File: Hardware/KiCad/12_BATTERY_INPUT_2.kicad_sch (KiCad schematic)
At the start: 0 parts

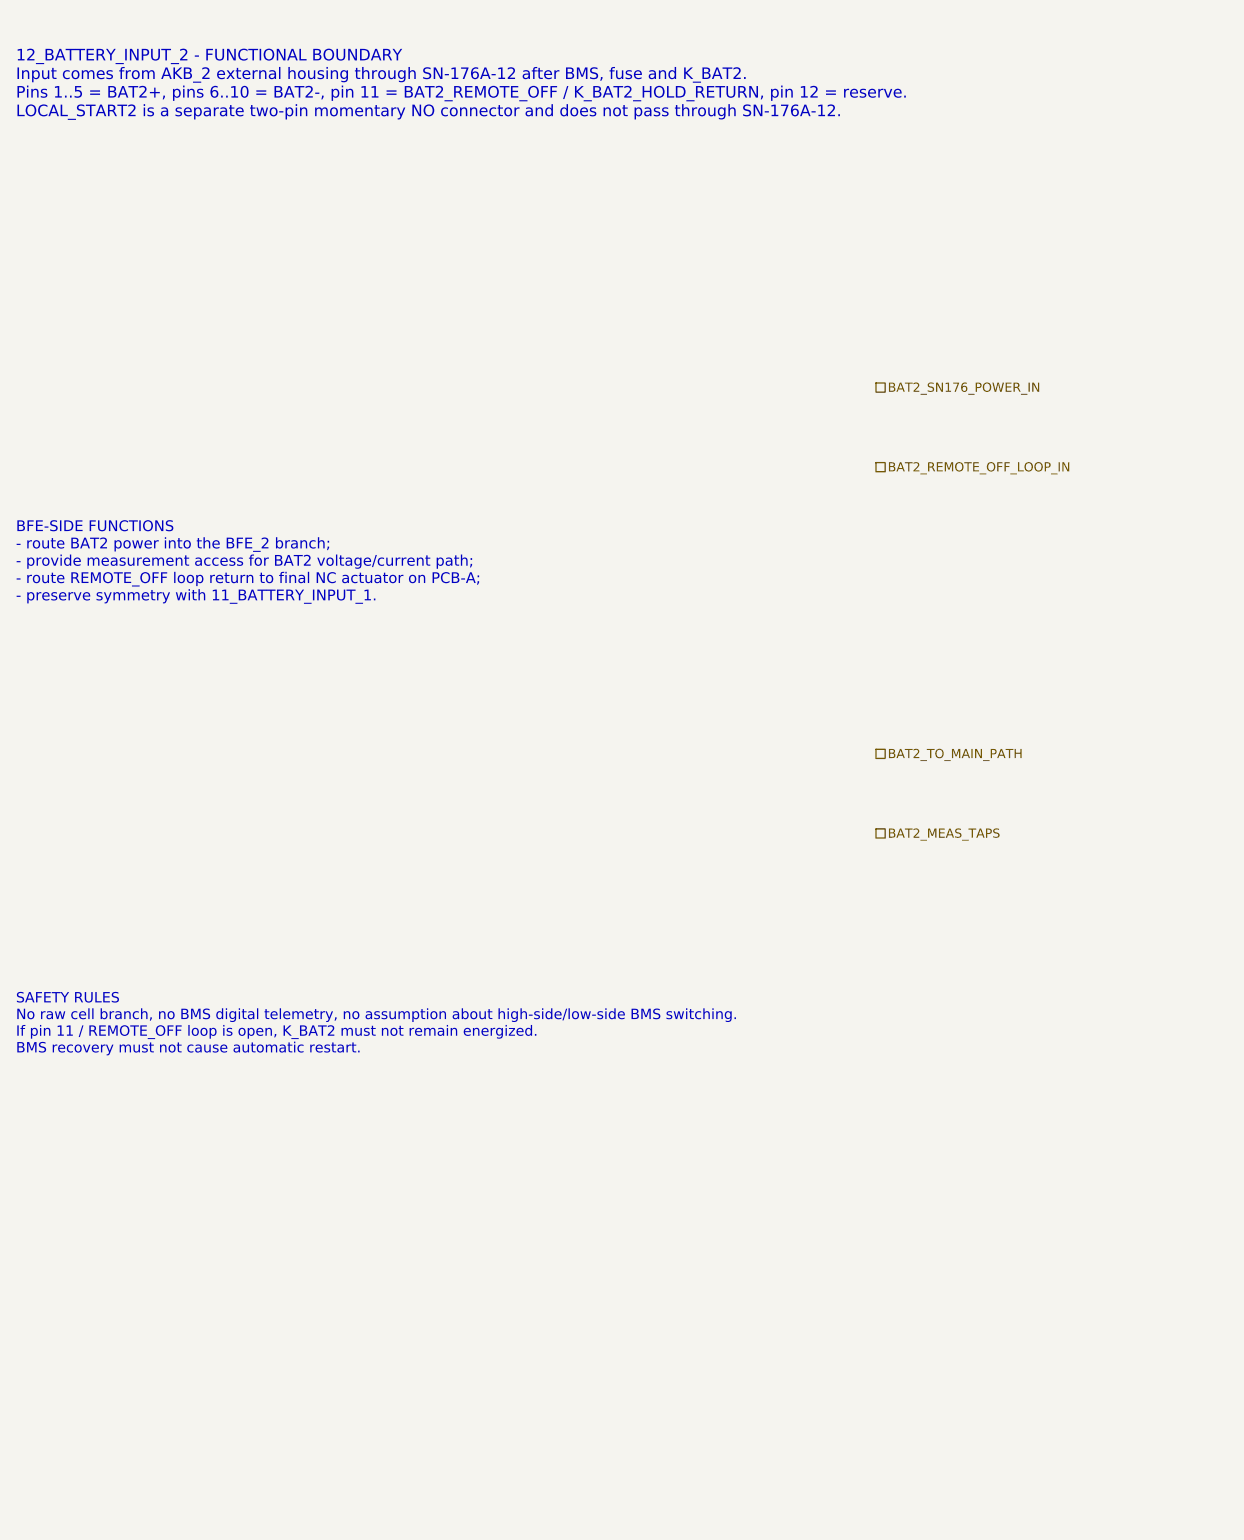
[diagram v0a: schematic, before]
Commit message: hardware: refine BFE inputs and hold-loop logic level B
Refine the first critical BFE sheets to Architecture Level B without selecting concrete components.

Included:
- BAT1/BAT2 SN-176A-12 positive/negative interface groups
- BAT1/BAT2 hold-loop return names
- hold-loop safe-state chain through EXT_KILL_NC and REMOTE_OFF_NC
- manifest update

No part numbers, footprints, PCB layout, relay technology, fuse values, current sensors or K_BATx/MAIN_SWx models are selected.
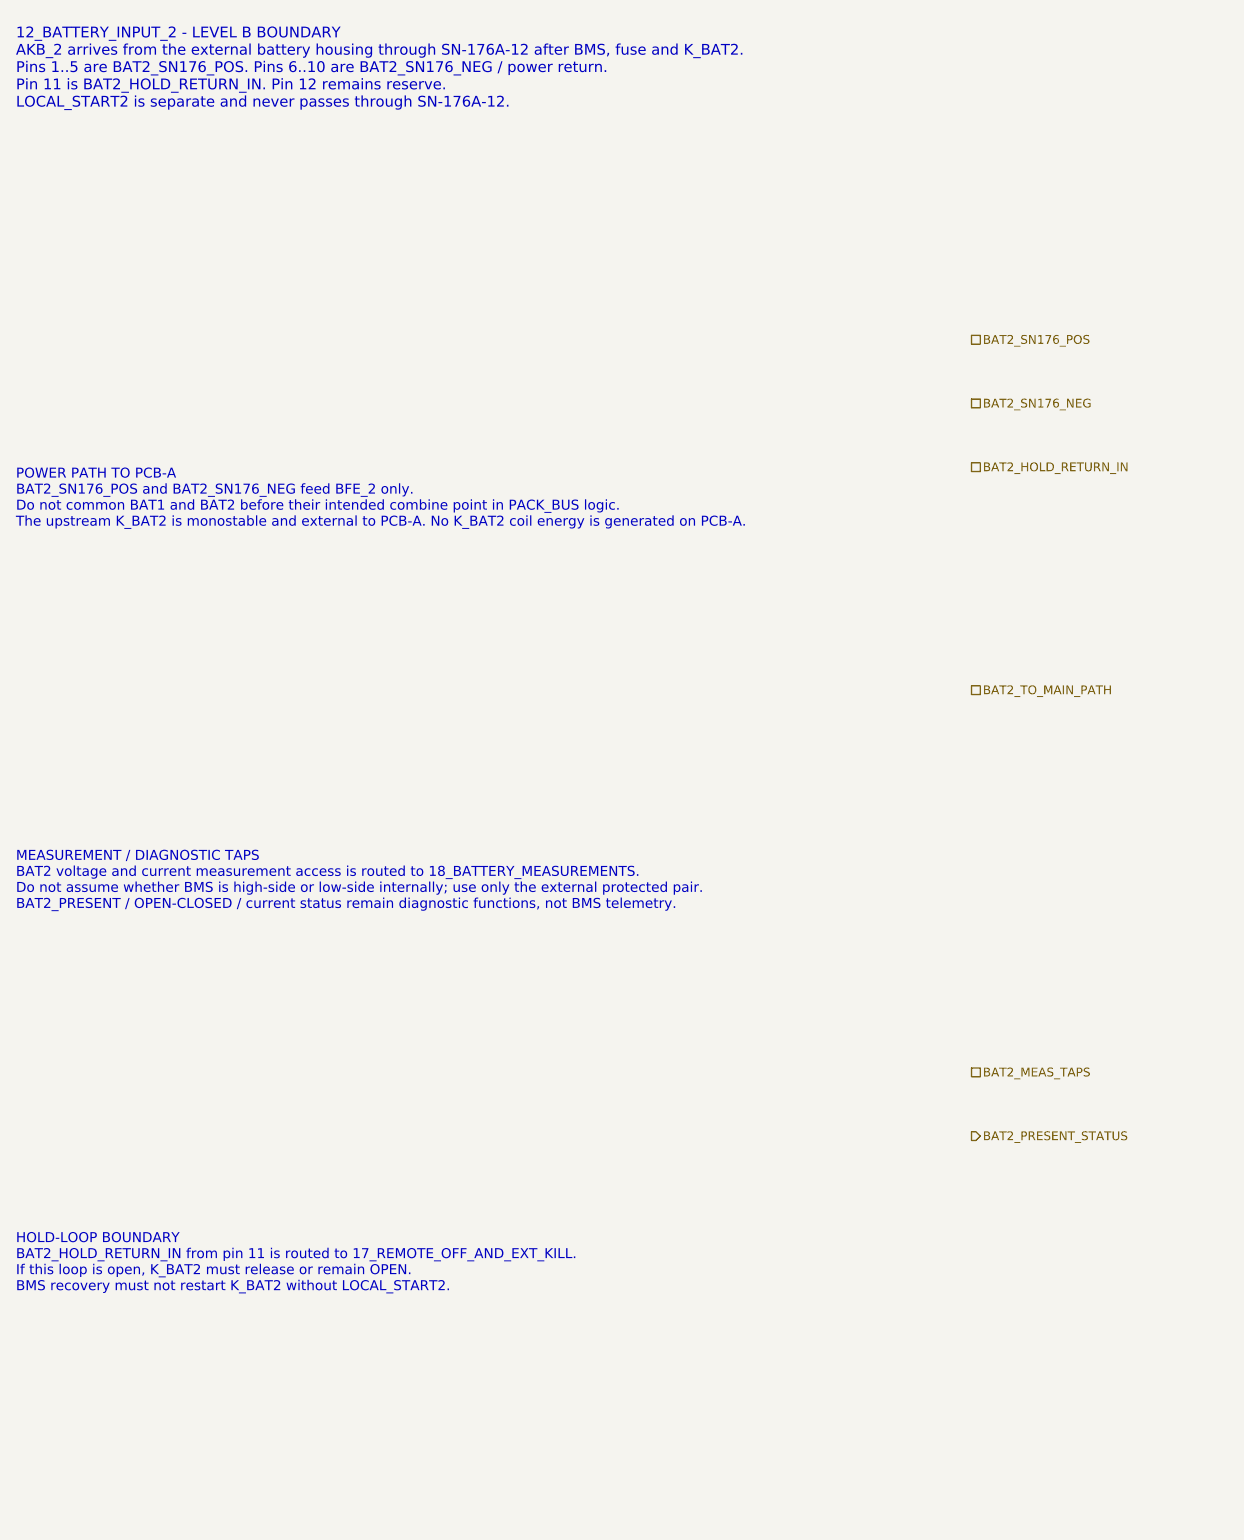
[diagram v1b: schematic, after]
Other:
- note added: "12_BATTERY_INPUT_2 - LEVEL B BOUNDARY AKB_2 arrives from the external battery housing through SN-176A-12 after BMS, fuse and K_BAT2. Pins 1..5 are BAT2_SN176_POS. Pins 6..10 are BAT2_SN176_NEG / power return. Pin 11 is BAT2_HOLD_RETURN_IN. Pin 12 remains reserve. LOCAL_START2 is separate and never passes through SN-176A-12."
- note added: "HOLD-LOOP BOUNDARY BAT2_HOLD_RETURN_IN from pin 11 is routed to 17_REMOTE_OFF_AND_EXT_KILL. If this loop is open, K_BAT2 must release or remain OPEN. BMS recovery must not restart K_BAT2 without LOCAL_START2."
- note added: "MEASUREMENT / DIAGNOSTIC TAPS BAT2 voltage and current measurement access is routed to 18_BATTERY_MEASUREMENTS. Do not assume whether BMS is high-side or low-side internally; use only the external protected pair. BAT2_PRESENT / OPEN-CLOSED / current status remain diagnostic functions, not BMS telemetry."
- note added: "POWER PATH TO PCB-A BAT2_SN176_POS and BAT2_SN176_NEG feed BFE_2 only. Do not common BAT1 and BAT2 before their intended combine point in PACK_BUS logic. The upstream K_BAT2 is monostable and external to PCB-A. No K_BAT2 coil energy is generated on PCB-A."
- note removed: "12_BATTERY_INPUT_2 - FUNCTIONAL BOUNDARY Input comes from AKB_2 external housing through SN-176A-12 after BMS, fuse and K_BAT2. Pins 1..5 = BAT2+, pins 6..10 = BAT2-, pin 11 = BAT2_REMOTE_OFF / K_BAT2_HOLD_RETURN, pin 12 = reserve. LOCAL_START2 is a separate two-pin momentary NO connector and does not pass through SN-176A-12."
- note removed: "BFE-SIDE FUNCTIONS - route BAT2 power into the BFE_2 branch; - provide measurement access for BAT2 voltage/current path; - route REMOTE_OFF loop return to final NC actuator on PCB-A; - preserve symmetry with 11_BATTERY_INPUT_1."
- note removed: "SAFETY RULES No raw cell branch, no BMS digital telemetry, no assumption about high-side/low-side BMS switching. If pin 11 / REMOTE_OFF loop is open, K_BAT2 must not remain energized. BMS recovery must not cause automatic restart."
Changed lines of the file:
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@@
 		(title "12_BATTERY_INPUT_2 - BFE input from AKB_2")
 		(date "2026-07-15")
-		(rev "A1")
+		(rev "B1")
 		(company "Gonoboben/plataVM")
-		(comment 1 "Architecture Level A: BFE-side input boundary for battery 2")
+		(comment 1 "Architecture Level B: BAT2 connector boundary and net naming")
 		(comment 2 "Symmetric to 11_BATTERY_INPUT_1")
 	)
-	(text "12_BATTERY_INPUT_2 - FUNCTIONAL BOUNDARY\nInput comes from AKB_2 external housing through SN-176A-12 after BMS, fuse and K_BAT2.\nPins 1..5 = BAT2+, pins 6..10 = BAT2-, pin 11 = BAT2_REMOTE_OFF / K_BAT2_HOLD_RETURN, pin 12 = reserve.\nLOCAL_START2 is a separate two-pin momentary NO connector and does not pass through SN-176A-12."
+	(text "12_BATTERY_INPUT_2 - LEVEL B BOUNDARY\nAKB_2 arrives from the external battery housing through SN-176A-12 after BMS, fuse and K_BAT2.\nPins 1..5 are BAT2_SN176_POS. Pins 6..10 are BAT2_SN176_NEG / power return.\nPin 11 is BAT2_HOLD_RETURN_IN. Pin 12 remains reserve.\nLOCAL_START2 is separate and never passes through SN-176A-12."
 		(exclude_from_sim no)
-		(at 12 18 0)
-		(effects (font (size 1.45 1.45)) (justify left))
+		(at 12 16 0)
+		(effects (font (size 1.35 1.35)) (justify left))
 		(uuid "bfe-dh-00000012-0000-4000-8000-000000000101")
 	)
-	(text "BFE-SIDE FUNCTIONS\n- route BAT2 power into the BFE_2 branch;\n- provide measurement access for BAT2 voltage/current path;\n- route REMOTE_OFF loop return to final NC actuator on PCB-A;\n- preserve symmetry with 11_BATTERY_INPUT_1."
+	(text "POWER PATH TO PCB-A\nBAT2_SN176_POS and BAT2_SN176_NEG feed BFE_2 only.\nDo not common BAT1 and BAT2 before their intended combine point in PACK_BUS logic.\nThe upstream K_BAT2 is monostable and external to PCB-A. No K_BAT2 coil energy is generated on PCB-A."
 		(exclude_from_sim no)
-		(at 12 78 0)
-		(effects (font (size 1.35 1.35)) (justify left))
+		(at 12 70 0)
+		(effects (font (size 1.25 1.25)) (justify left))
 		(uuid "bfe-dh-00000012-0000-4000-8000-000000000102")
 	)
-	(text "SAFETY RULES\nNo raw cell branch, no BMS digital telemetry, no assumption about high-side/low-side BMS switching.\nIf pin 11 / REMOTE_OFF loop is open, K_BAT2 must not remain energized.\nBMS recovery must not cause automatic restart."
+	(text "MEASUREMENT / DIAGNOSTIC TAPS\nBAT2 voltage and current measurement access is routed to 18_BATTERY_MEASUREMENTS.\nDo not assume whether BMS is high-side or low-side internally; use only the external protected pair.\nBAT2_PRESENT / OPEN-CLOSED / current status remain diagnostic functions, not BMS telemetry."
 		(exclude_from_sim no)
-		(at 12 136 0)
-		(effects (font (size 1.3 1.3)) (justify left))
+		(at 12 118 0)
+		(effects (font (size 1.25 1.25)) (justify left))
 		(uuid "bfe-dh-00000012-0000-4000-8000-000000000103")
 	)
-	(hierarchical_label "BAT2_SN176_POWER_IN" (shape passive) (exclude_from_sim no) (at 120 56 0) (effects (font (size 1.15 1.15)) (justify left)) (uuid "bfe-dh-00000012-0000-4000-8000-000000000201"))
-	(hierarchical_label "BAT2_REMOTE_OFF_LOOP_IN" (shape passive) (exclude_from_sim no) (at 120 66 0) (effects (font (size 1.15 1.15)) (justify left)) (uuid "bfe-dh-00000012-0000-4000-8000-000000000202"))
-	(hierarchical_label "BAT2_TO_MAIN_PATH" (shape passive) (exclude_from_sim no) (at 120 102 0) (effects (font (size 1.15 1.15)) (justify left)) (uuid "bfe-dh-00000012-0000-4000-8000-000000000203"))
-	(hierarchical_label "BAT2_MEAS_TAPS" (shape passive) (exclude_from_sim no) (at 120 112 0) (effects (font (size 1.15 1.15)) (justify left)) (uuid "bfe-dh-00000012-0000-4000-8000-000000000204"))
+	(text "HOLD-LOOP BOUNDARY\nBAT2_HOLD_RETURN_IN from pin 11 is routed to 17_REMOTE_OFF_AND_EXT_KILL.\nIf this loop is open, K_BAT2 must release or remain OPEN.\nBMS recovery must not restart K_BAT2 without LOCAL_START2."
+		(exclude_from_sim no)
+		(at 12 166 0)
+		(effects (font (size 1.25 1.25)) (justify left))
+		(uuid "bfe-dh-00000012-0000-4000-8000-000000000104")
+	)
+	(hierarchical_label "BAT2_SN176_POS" (shape passive) (exclude_from_sim no) (at 132 50 0) (effects (font (size 1.1 1.1)) (justify left)) (uuid "bfe-dh-00000012-0000-4000-8000-000000000201"))
+	(hierarchical_label "BAT2_SN176_NEG" (shape passive) (exclude_from_sim no) (at 132 58 0) (effects (font (size 1.1 1.1)) (justify left)) (uuid "bfe-dh-00000012-0000-4000-8000-000000000202"))
+	(hierarchical_label "BAT2_HOLD_RETURN_IN" (shape passive) (exclude_from_sim no) (at 132 66 0) (effects (font (size 1.1 1.1)) (justify left)) (uuid "bfe-dh-00000012-0000-4000-8000-000000000203"))
+	(hierarchical_label "BAT2_TO_MAIN_PATH" (shape passive) (exclude_from_sim no) (at 132 94 0) (effects (font (size 1.1 1.1)) (justify left)) (uuid "bfe-dh-00000012-0000-4000-8000-000000000204"))
+	(hierarchical_label "BAT2_MEAS_TAPS" (shape passive) (exclude_from_sim no) (at 132 142 0) (effects (font (size 1.1 1.1)) (justify left)) (uuid "bfe-dh-00000012-0000-4000-8000-000000000205"))
+	(hierarchical_label "BAT2_PRESENT_STATUS" (shape output) (exclude_from_sim no) (at 132 150 0) (effects (font (size 1.1 1.1)) (justify left)) (uuid "bfe-dh-00000012-0000-4000-8000-000000000206"))
 )
